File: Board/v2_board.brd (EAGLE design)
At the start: 78 x 78 mm, 31 parts, among them T3 BC337, U1 LF33CDT-TR, U2 ESP12, X2 MSTBA11

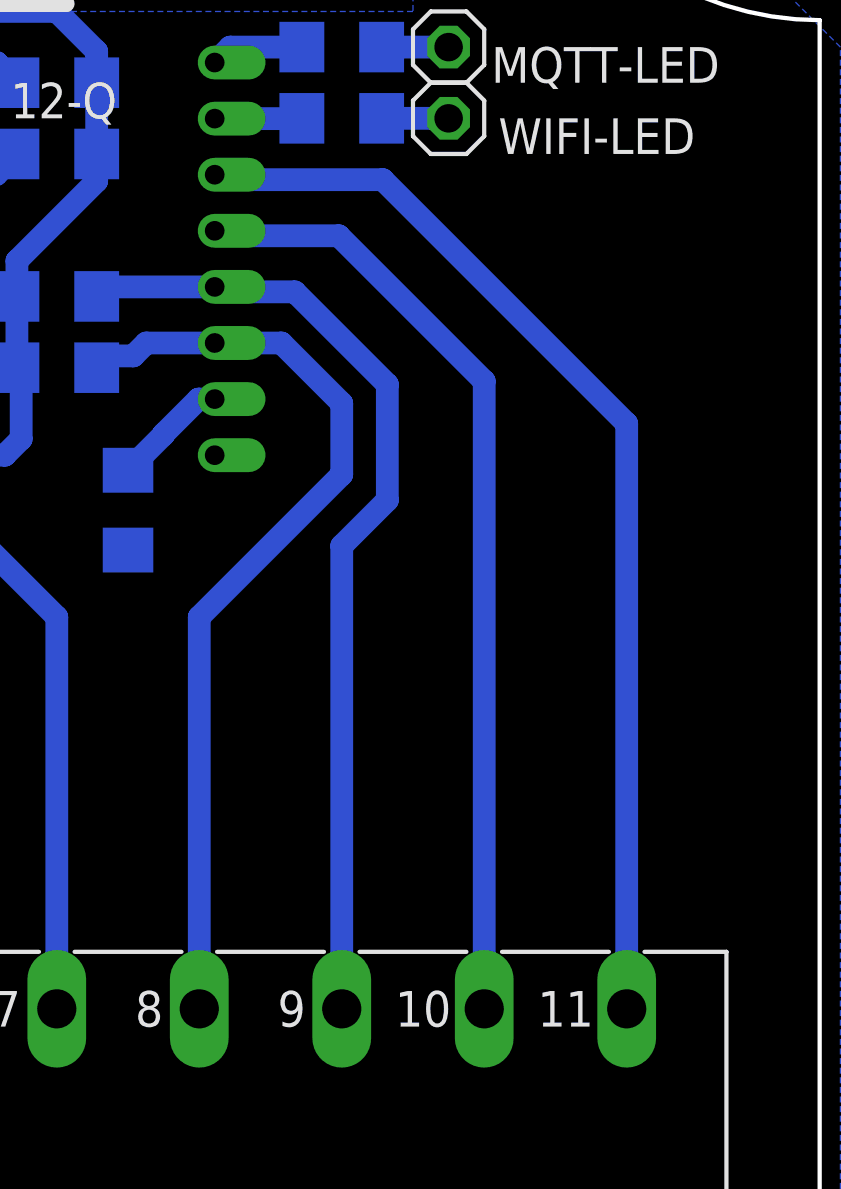
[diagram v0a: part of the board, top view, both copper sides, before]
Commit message: fixed library esp12
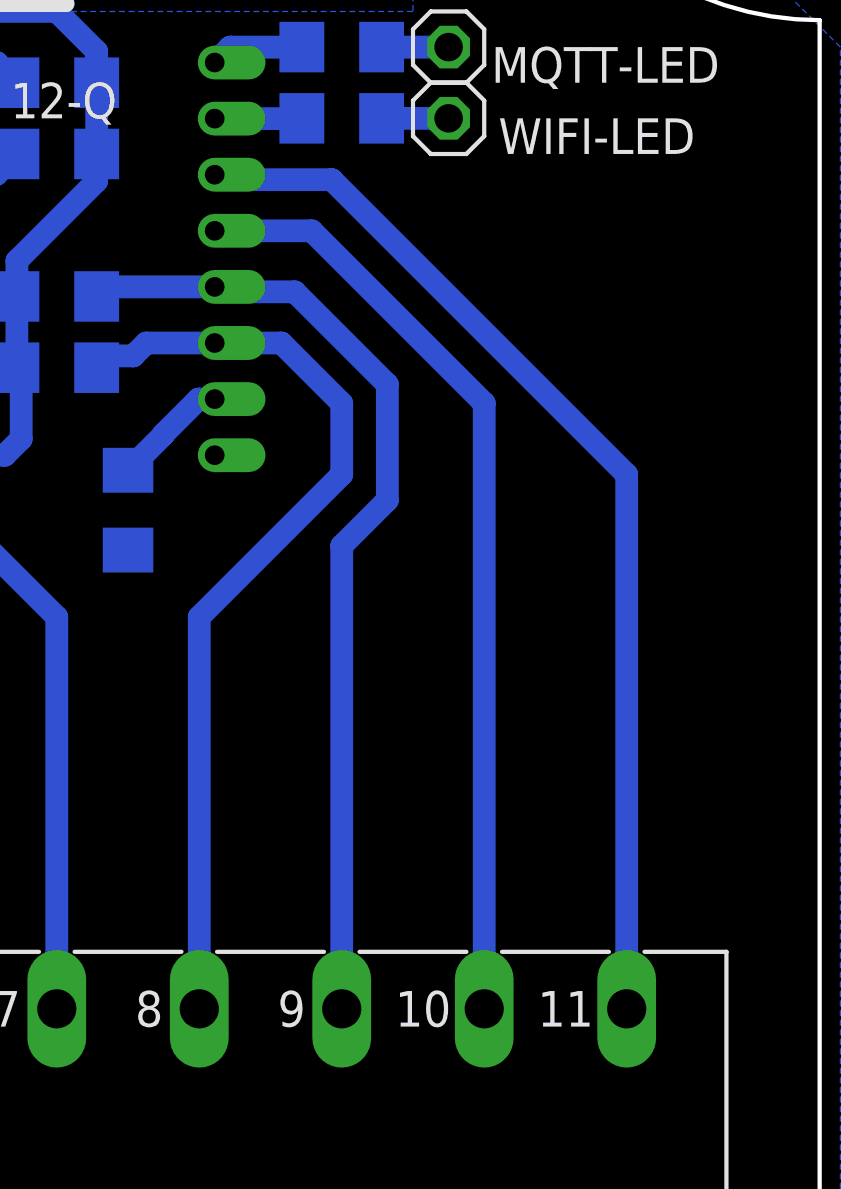
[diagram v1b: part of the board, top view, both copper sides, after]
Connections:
- net GPIO4: now also U2.GPIO5, X2.10; no longer U2.GPIO4, X2.11
- net GPIO5: now also U2.GPIO4, X2.11; no longer U2.GPIO5, X2.10
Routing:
- net GPIO4: track 39.2 -> 33.7 mm
- net GPIO5: track 34.2 -> 38.2 mm
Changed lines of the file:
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@@
 <setting verticaltext="up"/>
 </settings>
-<grid distance="1" unitdist="mm" unit="mm" style="lines" multiple="1" display="no" altdistance="5" altunitdist="mil" altunit="mil"/>
+<grid distance="50" unitdist="mil" unit="mil" style="lines" multiple="1" display="no" altdistance="5" altunitdist="mil" altunit="mil"/>
 <layers>
 <layer number="1" name="Top" color="4" fill="1" visible="yes" active="yes"/>
@@
 </element>
 <element name="BUZZER" library="pinhead" library_urn="urn:adsk.eagle:library:325" package="1X02" package3d_urn="urn:adsk.eagle:package:22435/2" value="" x="21.59" y="44.45"/>
-<element name="U2" library="esp826612q" package="ESP12" value="ESP12" x="49.53" y="59.69"/>
+<element name="U2" library="esp826612q" package="ESP12" value="ESP12" x="49.53" y="59.69">
+<attribute name="SPICEPREFIX" value="X" x="49.53" y="59.69" size="1.778" layer="27" display="off"/>
+</element>
 <element name="12V_IN" library="con-phoenix-508" library_urn="urn:adsk.eagle:library:176" package="MSTBA2" package3d_urn="urn:adsk.eagle:package:9615/1" value="MSTBA2" x="10.16" y="26.67">
 <attribute name="MF" value="FARNELL" x="10.16" y="26.67" size="1.778" layer="27" display="off"/>
@@
 </signal>
 <signal name="GPIO4">
+<contactref element="X2" pad="10"/>
+<wire x1="59.89" y1="59.49" x2="66.04" y2="53.34" width="0.8128" layer="16"/>
+<wire x1="66.04" y1="53.34" x2="66.04" y2="31.75" width="0.8128" layer="16"/>
+<contactref element="U2" pad="GPIO5"/>
+<wire x1="56.43" y1="59.49" x2="59.89" y2="59.49" width="0.8128" layer="16"/>
+</signal>
+<signal name="GPIO5">
+<contactref element="X2" pad="11"/>
+<wire x1="71.12" y1="31.75" x2="71.12" y2="50.8" width="0.8128" layer="16"/>
+<wire x1="56.6068" y1="61.3132" x2="60.6068" y2="61.3132" width="0.8128" layer="16"/>
+<wire x1="71.12" y1="50.8" x2="60.6068" y2="61.3132" width="0.8128" layer="16"/>
 <contactref element="U2" pad="GPIO4"/>
-<contactref element="X2" pad="11"/>
 <wire x1="56.43" y1="61.49" x2="56.6068" y2="61.3132" width="0.8128" layer="16"/>
-<wire x1="56.6068" y1="61.3132" x2="62.42365" y2="61.3132" width="0.8128" layer="16"/>
-<wire x1="62.42365" y1="61.3132" x2="71.12" y2="52.61685" width="0.8128" layer="16"/>
-<wire x1="71.12" y1="52.61685" x2="71.12" y2="31.75" width="0.8128" layer="16"/>
-</signal>
-<signal name="GPIO5">
-<contactref element="U2" pad="GPIO5"/>
-<contactref element="X2" pad="10"/>
-<wire x1="56.43" y1="59.49" x2="56.6068" y2="59.3132" width="0.8128" layer="16"/>
-<wire x1="56.6068" y1="59.3132" x2="60.8547" y2="59.3132" width="0.8128" layer="16"/>
-<wire x1="60.8547" y1="59.3132" x2="66.04" y2="54.1279" width="0.8128" layer="16"/>
-<wire x1="66.04" y1="54.1279" x2="66.04" y2="31.75" width="0.8128" layer="16"/>
 </signal>
 <signal name="GPIO0">

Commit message: Update
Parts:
- 12V_IN: value MSTBA2 -> (none)
- J1: value MSTBA11 -> (none)
- renumbered X2 to J1
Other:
- board text added: "TCLK"
- board text added: "TCS"
- board text added: "TDO"
- board text added: "TGND"
- board text removed: "MGND"
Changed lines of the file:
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@@
 <text x="44" y="21" size="1.778" layer="21" rot="R270">1WIRE</text>
 <text x="49.53" y="20.955" size="1.778" layer="21" rot="R270">ADC</text>
-<text x="69.85" y="20.955" size="1.778" layer="21" rot="R270">MGND</text>
+<text x="69.85" y="20.955" size="1.778" layer="21" rot="R270">TGND</text>
+<text x="64.77" y="20.955" size="1.778" layer="21" rot="R270">TCLK</text>
+<text x="59.69" y="20.955" size="1.778" layer="21" rot="R270">TCS</text>
+<text x="54.61" y="20.955" size="1.778" layer="21" rot="R270">TDO</text>
 </plain>
 <attributes>
@@
 <attribute name="SPICEPREFIX" value="X" x="49.53" y="59.69" size="1.778" layer="27" display="off"/>
 </element>
-<element name="12V_IN" library="con-phoenix-508" library_urn="urn:adsk.eagle:library:176" package="MSTBA2" package3d_urn="urn:adsk.eagle:package:9615/1" value="MSTBA2" x="10.16" y="26.67">
+<element name="12V_IN" library="con-phoenix-508" library_urn="urn:adsk.eagle:library:176" package="MSTBA2" package3d_urn="urn:adsk.eagle:package:9615/1" value="" x="10.16" y="26.67">
 <attribute name="MF" value="FARNELL" x="10.16" y="26.67" size="1.778" layer="27" display="off"/>
 <attribute name="MPN" value="1757242" x="10.16" y="26.67" size="1.778" layer="27" display="off"/>
@@
 <attribute name="OC_NEWARK" value="71C4161" x="10.16" y="26.67" size="1.778" layer="27" display="off"/>
 </element>
-<element name="X2" library="con-phoenix-508" library_urn="urn:adsk.eagle:library:176" package="MSTBA11" package3d_urn="urn:adsk.eagle:package:9621/1" value="MSTBA11" x="45.72" y="26.67">
+<element name="J1" library="con-phoenix-508" library_urn="urn:adsk.eagle:library:176" package="MSTBA11" package3d_urn="urn:adsk.eagle:package:9621/1" value="" x="45.72" y="26.67">
 <attribute name="MF" value="" x="45.72" y="26.67" size="1.778" layer="27" display="off"/>
 <attribute name="MPN" value="" x="45.72" y="26.67" size="1.778" layer="27" display="off"/>
@@
 <wire x1="16.5227625" y1="63.487234375" x2="20.89834375" y2="67.31" width="0.8128" layer="16"/>
 <wire x1="20.89834375" y1="67.31" x2="40.4636" y2="67.31" width="0.8128" layer="16"/>
-<contactref element="X2" pad="3"/>
-<contactref element="X2" pad="4"/>
+<contactref element="J1" pad="3"/>
+<contactref element="J1" pad="4"/>
 <wire x1="30.48" y1="31.75" x2="35.56" y2="31.75" width="0.8128" layer="16"/>
 <wire x1="43.028" y1="26.67" x2="38.1" y2="26.67" width="0.8128" layer="16"/>
@@
 <via x="17.78" y="50.8" extent="1-16" drill="1" shape="octagon"/>
 <wire x1="17.78" y1="50.8" x2="12.7" y2="50.8" width="0.8128" layer="1"/>
-<contactref element="X2" pad="1"/>
-<contactref element="X2" pad="2"/>
+<contactref element="J1" pad="1"/>
+<contactref element="J1" pad="2"/>
 </signal>
 <signal name="ADC">
@@
 <wire x1="46.99" y1="63.5" x2="46.99" y2="49.53" width="0.8128" layer="1"/>
 <via x="46.99" y="49.53" extent="1-16" drill="1" shape="octagon"/>
-<contactref element="X2" pad="7"/>
+<contactref element="J1" pad="7"/>
 <wire x1="50.8" y1="45.72" x2="46.99" y2="49.53" width="0.8128" layer="16"/>
 <wire x1="50.8" y1="45.72" x2="50.8" y2="31.75" width="0.8128" layer="16"/>
@@
 <wire x1="44.45" y1="53.34" x2="44.45" y2="49.53" width="0.8128" layer="1"/>
 <via x="44.45" y="49.53" extent="1-16" drill="1" shape="octagon"/>
-<contactref element="X2" pad="6"/>
+<contactref element="J1" pad="6"/>
 <wire x1="45.872" y1="26.67" x2="45.72" y2="26.822" width="0.8128" layer="16"/>
 <wire x1="45.72" y1="26.822" x2="45.72" y2="31.75" width="0.8128" layer="16"/>
@@
 </signal>
 <signal name="GPIO4">
-<contactref element="X2" pad="10"/>
+<contactref element="J1" pad="10"/>
 <wire x1="59.89" y1="59.49" x2="66.04" y2="53.34" width="0.8128" layer="16"/>
 <wire x1="66.04" y1="53.34" x2="66.04" y2="31.75" width="0.8128" layer="16"/>
@@
 </signal>
 <signal name="GPIO5">
-<contactref element="X2" pad="11"/>
+<contactref element="J1" pad="11"/>
 <wire x1="71.12" y1="31.75" x2="71.12" y2="50.8" width="0.8128" layer="16"/>
 <wire x1="56.6068" y1="61.3132" x2="60.6068" y2="61.3132" width="0.8128" layer="16"/>
@@
 <wire x1="52.222" y1="57.15" x2="52.562" y2="57.49" width="0.8128" layer="16"/>
 <wire x1="52.562" y1="57.49" x2="56.43" y2="57.49" width="0.8128" layer="16"/>
-<contactref element="X2" pad="9"/>
+<contactref element="J1" pad="9"/>
 <wire x1="56.43" y1="57.49" x2="56.6068" y2="57.3132" width="0.8128" layer="16"/>
 <wire x1="56.6068" y1="57.3132" x2="59.28575" y2="57.3132" width="0.8128" layer="16"/>
@@
 <wire x1="53.52700625" y1="55.0293" x2="53.98770625" y2="55.49" width="0.8128" layer="16"/>
 <wire x1="53.98770625" y1="55.49" x2="56.43" y2="55.49" width="0.8128" layer="16"/>
-<contactref element="X2" pad="8"/>
+<contactref element="J1" pad="8"/>
 <wire x1="55.88" y1="31.75" x2="55.88" y2="45.72" width="0.8128" layer="16"/>
 <wire x1="55.88" y1="45.72" x2="60.96" y2="50.8" width="0.8128" layer="16"/>
@@
 <contactref element="D3" pad="C"/>
 <wire x1="31.75" y1="39.37" x2="35.56" y2="39.37" width="0.8128" layer="16"/>
-<contactref element="X2" pad="5"/>
-<wire x1="40.64" y1="35.56" x2="36.83" y2="39.37" width="0.8128" layer="16"/>
+<wire x1="36.83" y1="39.37" x2="40.64" y2="35.56" width="0.8128" layer="16"/>
 <wire x1="36.83" y1="39.37" x2="35.56" y2="39.37" width="0.8128" layer="16"/>
-<wire x1="40.64" y1="31.75" x2="40.64" y2="35.56" width="0.8128" layer="16"/>
+<contactref element="J1" pad="5"/>
+<wire x1="40.64" y1="35.56" x2="40.64" y2="31.75" width="0.8128" layer="16"/>
 </signal>
 <signal name="N$16">
